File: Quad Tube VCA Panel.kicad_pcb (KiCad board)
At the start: 2 copper layers, 162.6 x 128.5 mm, 0 parts

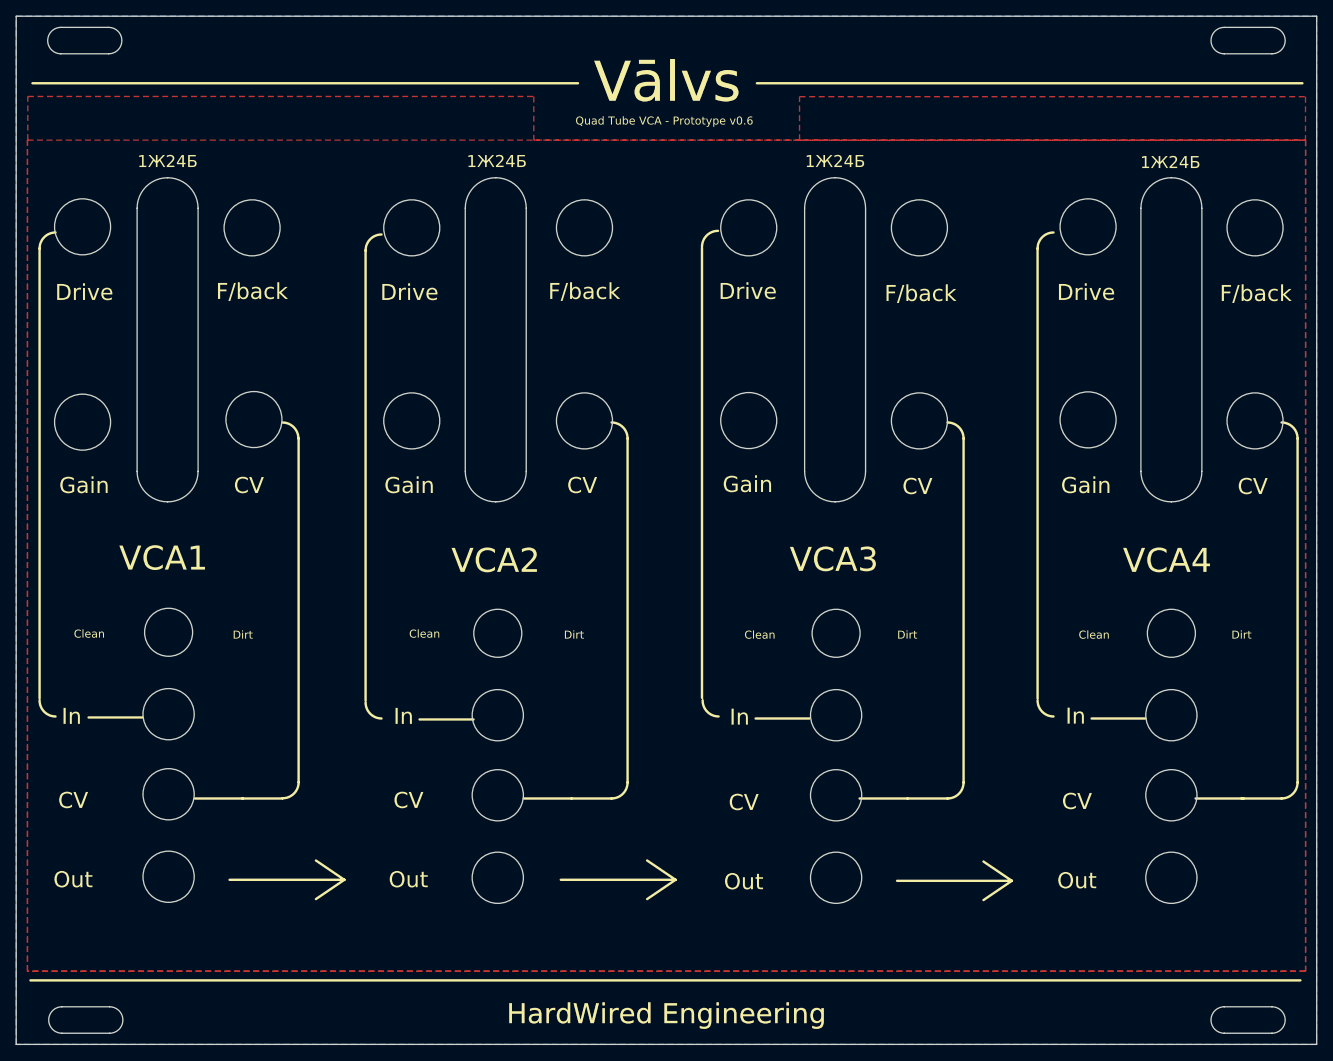
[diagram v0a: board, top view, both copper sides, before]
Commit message: tweaks panel pcb layers
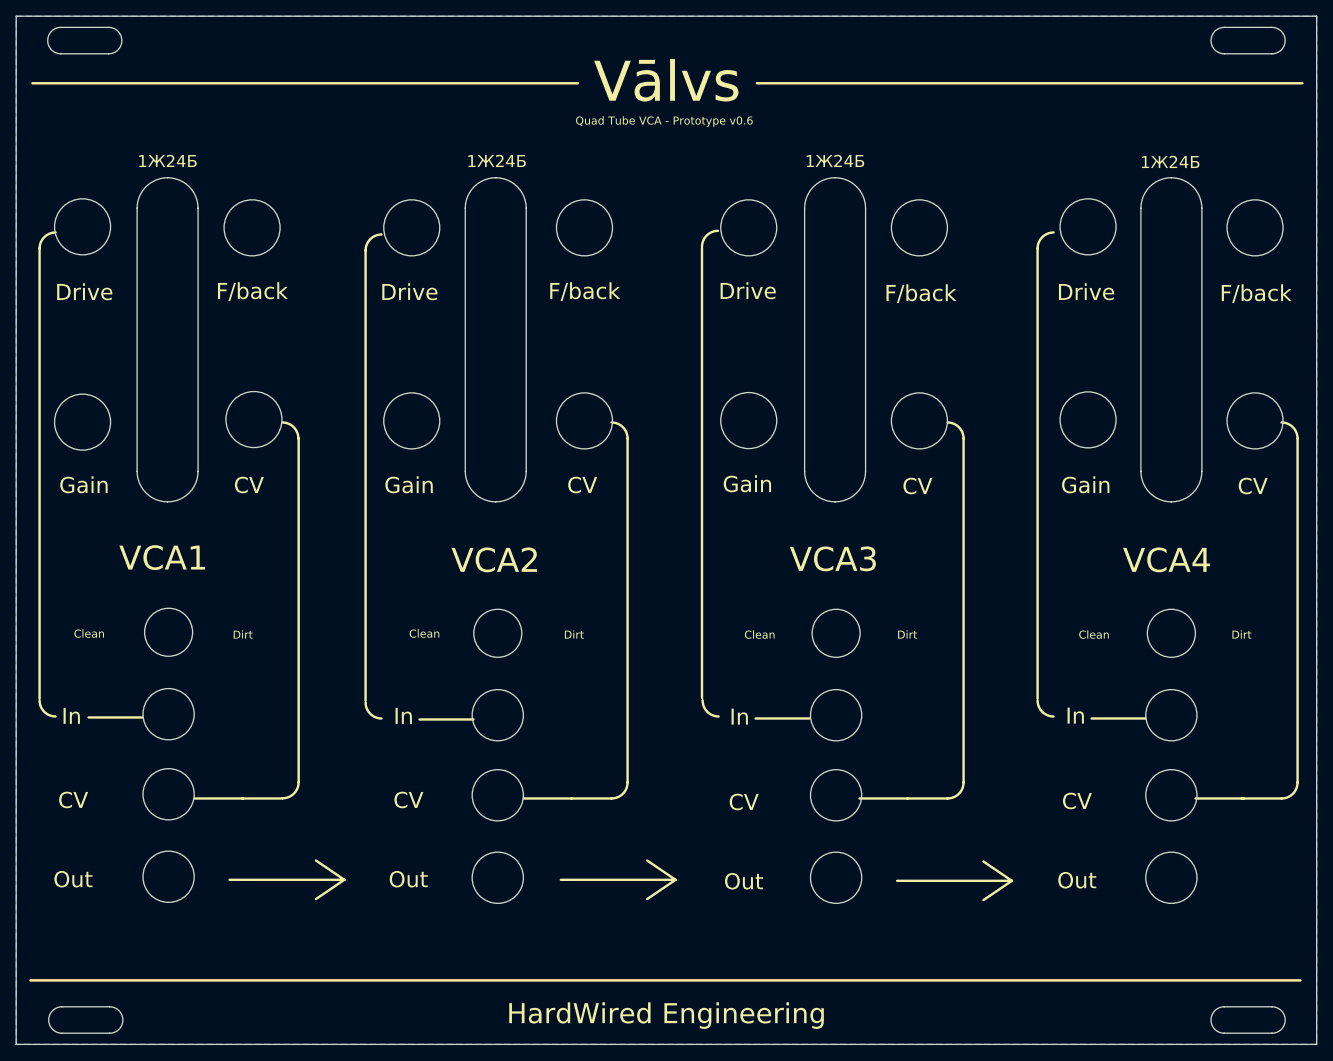
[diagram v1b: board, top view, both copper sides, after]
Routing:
- net (no net): track 0.00 -> 294.9 mm
- removed copper zone on F.Cu, net (none)

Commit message: adds copper to front of panel
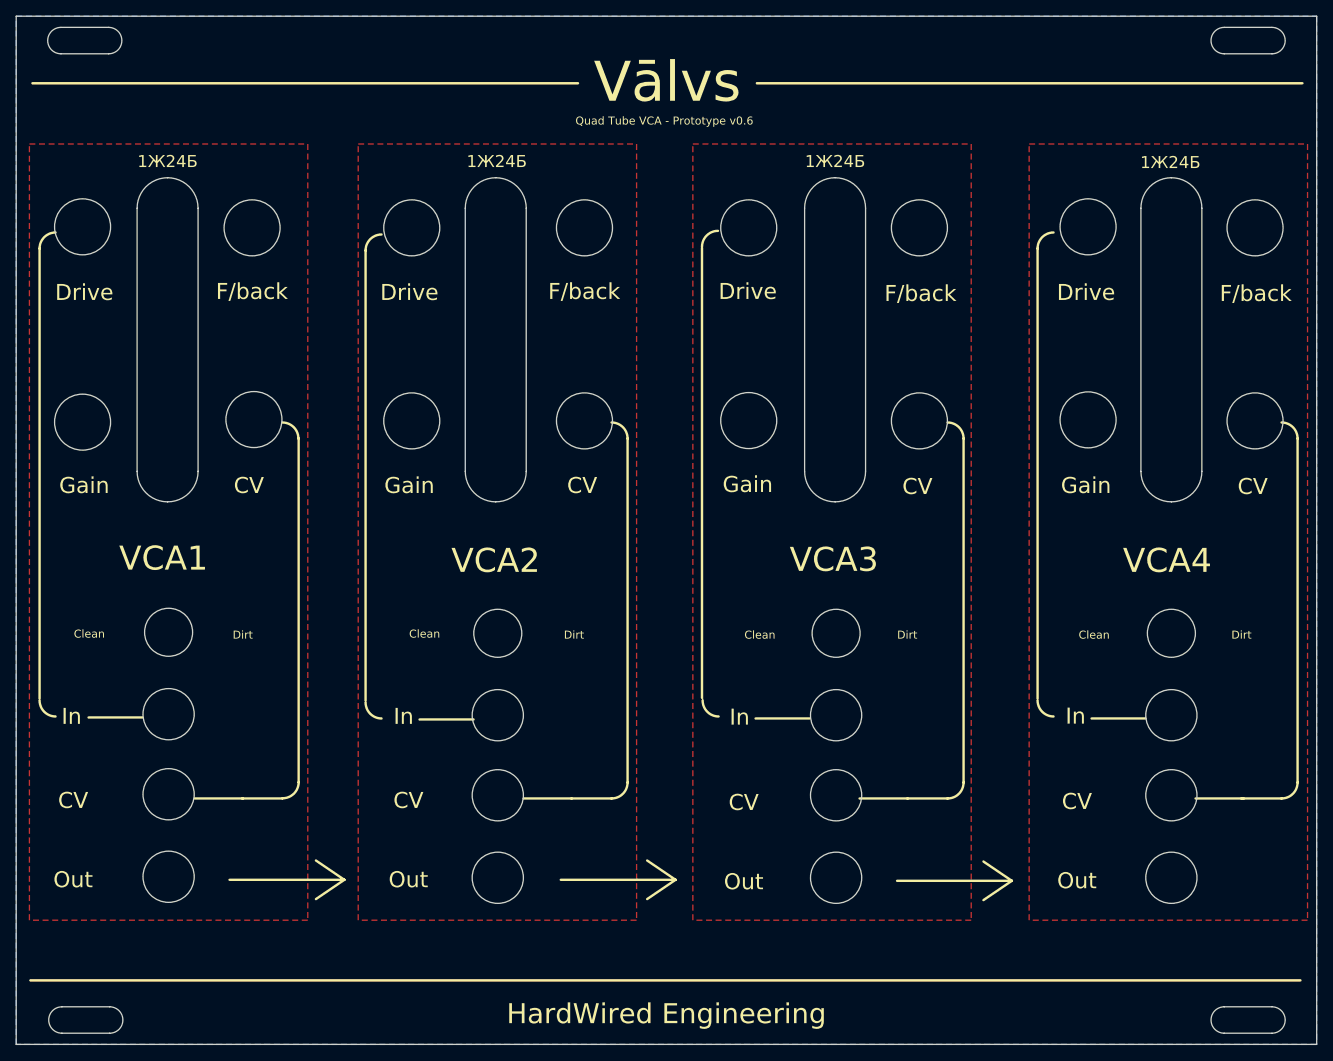
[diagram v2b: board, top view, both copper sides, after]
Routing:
- added copper zone on F.Cu, net (none)
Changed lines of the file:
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@@
+    )
+  )
+  (zone (net 0) (net_name "") (layer F.Cu) (hatch edge 0.508)
+    (connect_pads (clearance 0.508))
+    (min_thickness 0.254)
+    (fill yes (arc_segments 32) (thermal_gap 0.508) (thermal_bridge_width 0.508) (smoothing fillet) (radius 3))
+    (polygon
+      (pts
+        (xy 43.18 173.707825) (xy 8.382 173.707825) (xy 8.382 76.679825) (xy 43.18 76.679825)
+      )
+    )
+  )
+  (zone (net 0) (net_name "") (layer F.Cu) (hatch edge 0.508)
+    (connect_pads (clearance 0.508))
+    (min_thickness 0.254)
+    (fill yes (arc_segments 32) (thermal_gap 0.508) (thermal_bridge_width 0.508) (smoothing fillet) (radius 3))
+    (polygon
+      (pts
+        (xy 84.279251 173.707825) (xy 49.481251 173.707825) (xy 49.481251 76.679825) (xy 84.279251 76.679825)
+      )
+    )
+  )
+  (zone (net 0) (net_name "") (layer F.Cu) (hatch edge 0.508)
+    (connect_pads (clearance 0.508))
+    (min_thickness 0.254)
+    (fill yes (arc_segments 32) (thermal_gap 0.508) (thermal_bridge_width 0.508) (smoothing fillet) (radius 3))
+    (polygon
+      (pts
+        (xy 126.111 173.707825) (xy 91.313 173.707825) (xy 91.313 76.679825) (xy 126.111 76.679825)
+      )
+    )
+  )
+  (zone (net 0) (net_name "") (layer F.Cu) (hatch edge 0.508)
+    (connect_pads (clearance 0.508))
+    (min_thickness 0.254)
+    (fill yes (arc_segments 32) (thermal_gap 0.508) (thermal_bridge_width 0.508) (smoothing fillet) (radius 3))
+    (polygon
+      (pts
+        (xy 168.148 173.707825) (xy 133.35 173.707825) (xy 133.35 76.679825) (xy 168.148 76.679825)
+      )
     )
   )

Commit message: updates v0.6 gerbers
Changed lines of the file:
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@@
   (general
     (thickness 1.6)
-    (drawings 175)
+    (drawings 177)
     (tracks 4)
     (zones 0)
@@
     (uvia_drill 0.1)
   )
+  (gr_text "HardWired Engineering" (at 88.011 185.42) (layer F.Cu)
+    (effects (font (size 2.5 2.5) (thickness 0.25)))
+  )
+  (gr_text Vālvs (at 88.138 68.961) (layer F.Cu)
+    (effects (font (size 5 5) (thickness 0.5)))
+  )
   (gr_text Drive (at 55.88 95.25) (layer F.SilkS)
